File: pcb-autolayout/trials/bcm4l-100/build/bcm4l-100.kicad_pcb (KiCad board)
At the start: 4 copper layers, 80 x 60 mm, 128 parts, among them J1 MicroFit 2x4, J2 MicroFit 2x6, J3 SWD, Q1 SQD40P06 (P-MOS), Q11 ZXMP6A13F -60V, Q12 MMBT3904, Q13 ZXMP6A13F -60V, Q14 MMBT3904, Q15 ZXMP6A13F -60V, Q16 MMBT3904, Q17 ZXMP6A13F -60V, Q18 MMBT3904, SW1 RESET, U1 LMR16006X-Q1, U2 TLV1117LV33-Q1, U3 TJA1051T/3, U4 TJA1021T/20, U5 STM32F103C8T6, Y1 8MHz

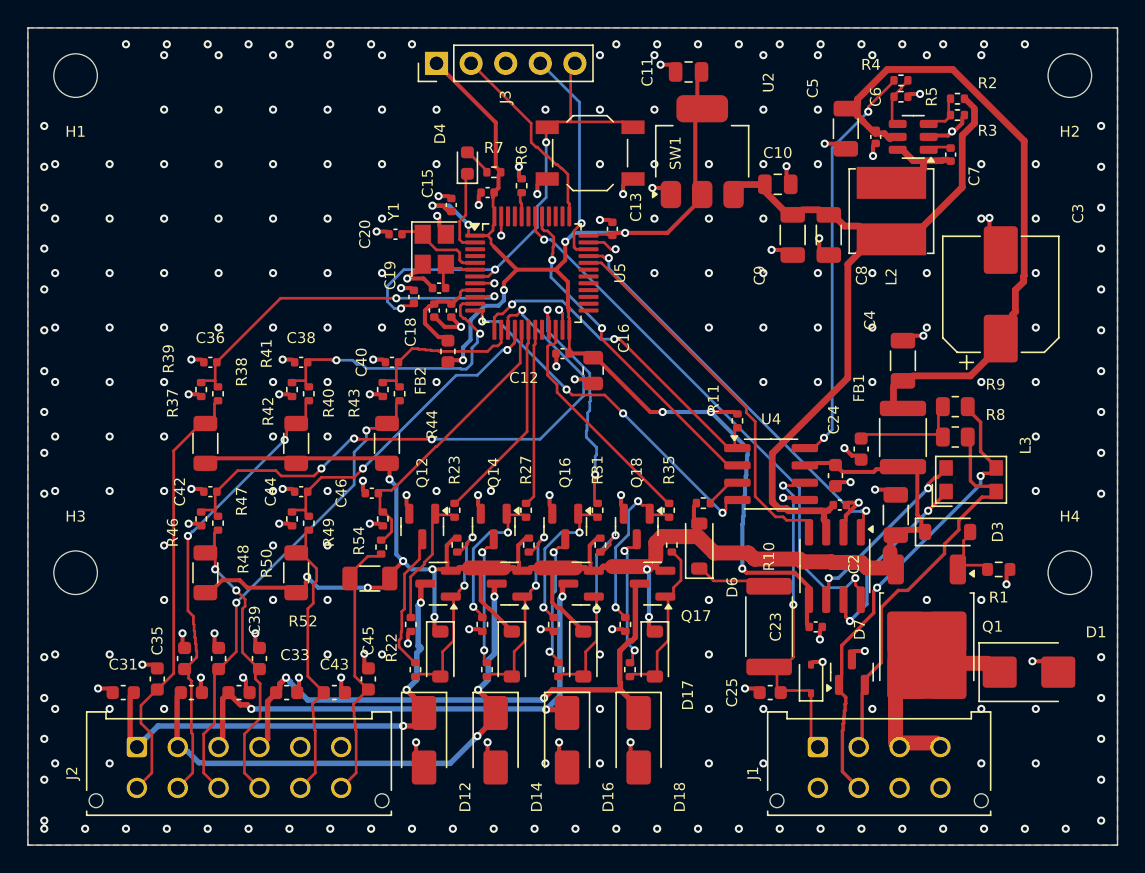
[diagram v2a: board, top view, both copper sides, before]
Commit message: pcb-autolayout: revert circuit to original, engine-computed netclasses
Circuit changes from round 3 reverted (circuit is an input, owner's
decision); review findings moved to CIRCUIT-ISSUES.md. circuit.py now
only adds layout constraints (net attributes, keep_away, rots, near).

Engine: T08/T09 netclass compiler (IPC-2221 width, voltage-based
clearance, per-kind minimums, KiCad netclasses in .kicad_pro, table
build/netclasses.md, tests); per-net current; plane-island measurement
before dead-copper removal; I/O protection placed before blocks;
satellite halo for anchors; TPS54202 template; cascading rip-up with
best-state restore and cycle detection.

Trial on original circuit: KiCad DRC 0 errors, 13/16 rules; 1 open pin
caused by regional capacity (needs T34 placement repair).

Co-Authored-By: Claude Opus 5.5 <noreply@anthropic.com>
Claude-Session: https://claude.ai/code/session_012jwodCpQFB8wopi3P3TnUz
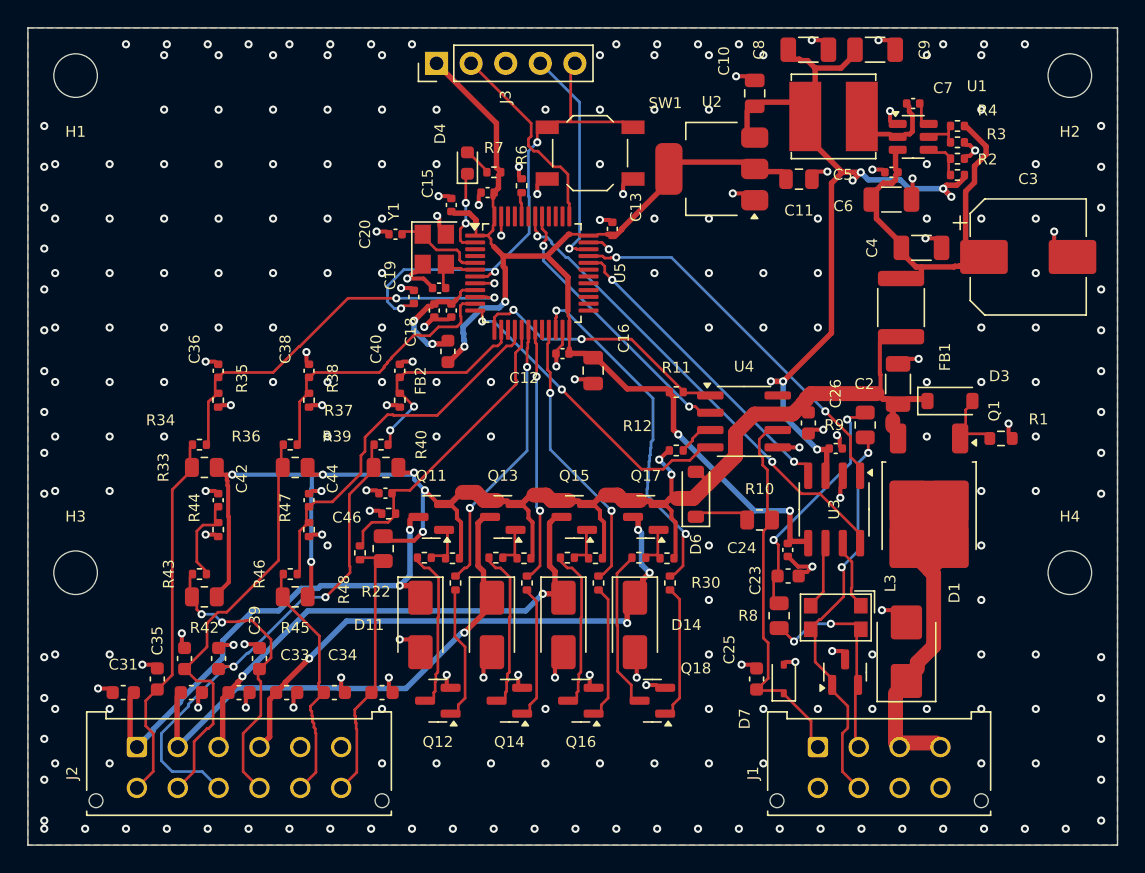
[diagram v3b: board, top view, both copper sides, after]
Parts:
- removed D17: BZT52C10, Diode_SMD:D_SOD-123
- removed the D3 at (167.5, 97.0)
- removed the D6 at (149.3, 98.0)
- removed the D7 at (157.5, 107.8)
- removed the R1 at (171.3, 99.8)
- removed the R10 at (154.4, 104.0)
- removed the R40 at (119.7, 90.5)
- removed the R49 at (119.7, 100.0)
- removed R52: 4k7, Resistor_SMD:R_1206_3216Metric
- removed the R8 at (168.1, 90.0)
- removed the R9 at (168.1, 87.8)
- added R34: 47k, Resistor_SMD:R_0402_1005Metric, F.Cu at (112.6, 90.6)
- added R35: 10k, Resistor_SMD:R_0402_1005Metric, F.Cu at (114.0, 87.3)
- added R44: 10k, Resistor_SMD:R_0402_1005Metric, F.Cu at (114.0, 96.8)
- C10: renamed from C11; value 22u -> 10u
- C11: renamed from C10; value 10u -> 22u
- C2, C6: value 100n 100V -> 100n 50V
- C20: renamed from C40; value 10n -> 20p
- C21: value 15p -> 20p
- C24: renamed from C26; value 100n 50V -> 4n7
- C26: renamed from C24; value 4n7 -> 100n 50V
- C3: value 47u 63V -> 47u 35V
- C4: value 2u2 100V -> 4u7 50V
- C40: renamed from C20; value 15p -> 10n
- C5: value 4u7 100V -> 10u 50V
- D1: value SMBJ33CA -> SMBJ24A
- D6: renamed from D11; value BZT52C10 -> BAS21
- D7: renamed from D15; value BZT52C10 -> ESD LIN; footprint Diode_SMD:D_SOD-123 -> Diode_SMD:D_SOD-323
- L2: value 22u -> 10u
- Q11, Q13, Q15, Q17: value ZXMP6A13F -60V -> AO3401A
- R1: renamed from R36; footprint Resistor_SMD:R_0402_1005Metric -> Resistor_SMD:R_0603_1608Metric
- R10: renamed from R5; value 100k -> 1k; footprint Resistor_SMD:R_0402_1005Metric -> Resistor_SMD:R_0805_2012Metric
- R11: renamed from R27; value 1k -> 4k7
- R2: renamed from R29; value 10k -> 100k
- R21: renamed from R50; value 82k -> 10k
- R22: renamed from R41; value 82k -> 10k
- R23: renamed from R53; value 82k -> 1k
- R26: renamed from R22; value 10k -> 1k
- R28: renamed from R23; value 1k -> 10k
- R29: renamed from R28; value 10k -> 1k
- R3: renamed from R31; value 1k -> 13k7
- R30: renamed from R7; value 1k -> 10k
- R32: renamed from R6; value 10k -> 1k
- R33: renamed from R35; value 1k -> 2k2; footprint Resistor_SMD:R_0402_1005Metric -> Resistor_SMD:R_0805_2012Metric
- R36: renamed from R12; value 10k -> 2k2; footprint Resistor_SMD:R_0402_1005Metric -> Resistor_SMD:R_0805_2012Metric
- R37, R43, R46: value 4k7 -> 47k; footprint Resistor_SMD:R_1206_3216Metric -> Resistor_SMD:R_0402_1005Metric
- R39: renamed from R4; value 10k -> 2k2; footprint Resistor_SMD:R_0402_1005Metric -> Resistor_SMD:R_0805_2012Metric
- R4: renamed from R32; value 10k -> 100k
- R40: renamed from R47; value 82k -> 47k
- R42: renamed from R34; value 10k -> 2k2; footprint Resistor_SMD:R_0402_1005Metric -> Resistor_SMD:R_0805_2012Metric
- R45: renamed from R33; value 10k -> 2k2; footprint Resistor_SMD:R_0402_1005Metric -> Resistor_SMD:R_0805_2012Metric
- R48: renamed from R11; value 4k7 -> 2k2; footprint Resistor_SMD:R_0402_1005Metric -> Resistor_SMD:R_0805_2012Metric
- R49: renamed from R38; value 82k -> 47k
- R5: renamed from R30; value 10k -> 22k
- R6: renamed from R44; value 82k -> 10k
- R7: renamed from R45; value 10k -> 1k
- R8: renamed from R2; value 100k -> 60R4; footprint Resistor_SMD:R_0402_1005Metric -> Resistor_SMD:R_0805_2012Metric
- R9: renamed from R3; value 18k -> 60R4; footprint Resistor_SMD:R_0402_1005Metric -> Resistor_SMD:R_0805_2012Metric
- U1: value LMR16006X-Q1 -> TPS54202
- U2: value TLV1117LV33-Q1 -> AMS1117-3.3
- moved R5 48.6 mm to (168.2, 68.4), turned to 0 degrees
- moved R39 47.3 mm to (126.3, 92.3), turned to 180 degrees
- moved R4 47.1 mm to (168.2, 67.2), turned to 180 degrees
- moved R8 40.1 mm to (155.2, 103.2), turned to 90 degrees
- moved R2 37.8 mm to (168.2, 70.8), turned to 180 degrees
- moved D3 37.1 mm to (167.7, 87.4), turned to 0 degrees
- moved R3 36.9 mm to (168.2, 69.6), turned to 0 degrees
- moved R33 34.3 mm to (113.0, 92.3), turned to 180 degrees
- moved R10 32.8 mm to (153.7, 96.1)
- moved R42 31.7 mm to (113.0, 101.8), turned to 180 degrees
- moved R32 31.1 mm to (147.1, 100.8), turned to -90 degrees
- moved R30 31.1 mm to (146.9, 98.9)
- moved R1 30.8 mm to (171.4, 90.1), turned to 0 degrees
- moved R36 30.1 mm to (119.6, 92.3)
- moved R45 27.9 mm to (119.6, 101.8), turned to 180 degrees
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- renumbered C9 to C8, C8 to C9, D12 to D11, D14 to D12, D16 to D13, D18 to D14, D13 to D3, R25 to R12, R54 to R25, R21 to R27, R26 to R31, R39 to R38, R51 to R41, R48 to R47, R42 to R50
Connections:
- C10 pad 1: +3V3 -> +5V
- C11 pad 1: +5V -> +3V3
- C20 pad 1: IN3_M -> OSC_IN
- C24 pad 1: VBAT_P -> CAN_SPL
- C26 pad 1: CAN_SPL -> VBAT_P
- C40 pad 1: OSC_IN -> IN3_M
- D3 pad 2: OUT2_G -> Q1_G
- D6 pad 1: VBAT_P -> LIN_PU
- D6 pad 2: OUT1_G -> VBAT_P
- D7 pad 1: VBAT_P -> LIN
- D7 pad 2: OUT3_G -> GND
- L3 pad 2: CANH -> CANL_T
- L3 pad 4: CANL_T -> CANH
- R1 pad 1: OUT4_B -> Q1_G
- R10 pad 1: EN5 -> LIN_PU
- R10 pad 2: GND -> LIN
- R11 pad 1: OUT2_M -> LIN_RX
- R11 pad 2: OUT2_B -> +3V3
- R12 pad 1: VBAT_P -> LIN_WAKE
- R12 pad 2: OUT2_G -> VBAT_P
- R2 pad 1: VBAT_P -> +5V
- R2 pad 2: OUT3_G -> FB5
- R21 pad 1: IN5 -> VBAT_P
- R21 pad 2: IN5_M -> OUT1_G
- R22 pad 1: IN2 -> OUT1_G
- R22 pad 2: IN2_M -> OUT1_C
- R23 pad 1: IN6 -> OUT1_M
- R23 pad 2: IN6_M -> OUT1_B
- R24 pad 1: OUT1_B -> VBAT_P
- R24 pad 2: GND -> OUT2_G
- R25 pad 1: IN6_M -> OUT2_G
- R25 pad 2: GND -> OUT2_C
- R26 pad 1: OUT1_G -> OUT2_M
- R26 pad 2: OUT1_C -> OUT2_B
- R27 pad 2: OUT1_G -> OUT3_G
- R28 pad 1: OUT1_M -> OUT3_G
- R28 pad 2: OUT1_B -> OUT3_C
- R29 pad 1: OUT2_B -> OUT3_M
- R29 pad 2: GND -> OUT3_B
- R3 pad 1: OUT3_M -> FB5
- R3 pad 2: OUT3_B -> GND
- R30 pad 1: +3V3 -> VBAT_P
- R30 pad 2: LED_A -> OUT4_G
- R31 pad 1: OUT2_G -> OUT4_G
- R31 pad 2: OUT2_C -> OUT4_C
- R32 pad 1: BOOT0 -> OUT4_M
- R32 pad 2: GND -> OUT4_B
- R33 pad 1: OUT4_M -> VBAT_P
- R33 pad 2: OUT4_B -> IN1
- R36 pad 1: LIN_WAKE -> VBAT_P
- R36 pad 2: VBAT_P -> IN2
- R37 pad 1: VBAT_P -> IN2
- R37 pad 2: IN1 -> IN2_M
- R38 pad 1: IN1_M -> IN2_M
- R39 pad 1: LIN_INH -> VBAT_P
- R39 pad 2: EN5 -> IN3
- R4 pad 1: OUT3_B -> VBAT_F
- R4 pad 2: GND -> EN5
- R40 pad 1: IN4 -> IN3
- R40 pad 2: IN4_M -> IN3_M
- R41 pad 1: IN5_M -> IN3_M
- R42 pad 1: OUT4_G -> VBAT_P
- R42 pad 2: OUT4_C -> IN4
- R43 pad 1: VBAT_P -> IN4
- R43 pad 2: IN3 -> IN4_M
- R45 pad 2: OUT4_G -> IN5
- R46 pad 1: VBAT_P -> IN5
- R46 pad 2: IN4 -> IN5_M
- R47 pad 1: IN4_M -> IN5_M
- R48 pad 1: LIN_RX -> VBAT_P
- R48 pad 2: +3V3 -> IN6
- R49 pad 1: IN1 -> IN6
- R49 pad 2: IN1_M -> IN6_M
- R5 pad 1: OUT3_G -> EN5
- R5 pad 2: OUT3_C -> GND
- R50 pad 1: IN2_M -> IN6_M
- R6 pad 1: IN3 -> BOOT0
- R6 pad 2: IN3_M -> GND
- R7 pad 1: IN3_M -> +3V3
- R7 pad 2: GND -> LED_A
- R8 pad 1: +5V -> CANH
- R8 pad 2: FB5 -> CAN_SPL
- R9 pad 1: FB5 -> CANL
- R9 pad 2: GND -> CAN_SPL
- U1 pad 1: BOOT5 -> GND
- U1 pad 2: GND -> SW5
- U1 pad 3: FB5 -> VBAT_F
- U1 pad 4: EN5 -> FB5
- U1 pad 5: VBAT_F -> EN5
- U1 pad 6: SW5 -> BOOT5
- U4 pad 8: LIN_INH -> (no net)
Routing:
- net IN4_M: track 41.9 -> 5.58 mm, vias 4 -> 0
- net LIN_INH: track 28.9 -> 0.00 mm, vias 2 -> 0
- net VBAT_F: track 40.8 -> 21.2 mm
- net +3V3: track 90.7 -> 74.7 mm, vias 9 -> 4
- net CANH: track 25.8 -> 12.8 mm, vias 0 -> 2
- net OUT3_G: track 14.5 -> 2.40 mm, vias 2 -> 0
- net OUT2_G: track 12.9 -> 2.40 mm, vias 2 -> 0
- net OUT1_G: track 12.9 -> 2.40 mm, vias 2 -> 0
- net CAN_SPL: track 6.50 -> 16.0 mm, vias 0 -> 2
- net OUT4_M: track 15.9 -> 25.3 mm, vias 0 -> 2
- net CANH_T: track 12.7 -> 3.69 mm, vias 2 -> 0
- net CANL_T: track 12.4 -> 3.55 mm, vias 2 -> 0
- net +5V: track 43.7 -> 51.8 mm, vias 0 -> 7
- net OUT4_G: track 10.2 -> 2.40 mm
- net VBAT_IN: track 9.30 -> 15.6 mm
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
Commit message: pcb-autolayout: seven phase skills + tools behind each
Skills: pcb-intake, pcb-part, pcb-constraints, pcb-place, pcb-route,
pcb-verify, pcb-release; pcb-autolayout becomes the orchestrator.

Tools:
- intake.py + pcbkit/sexpr.py: KiCad kicadsexpr netlist -> design.json
  (sheet = block, Layout_* fields); round-trip test, checked on a real
  KiCad 7 netlist (159/159 pins)
- verify.py: check an existing board (incl. hand-drawn) with the same
  rules; absolute pad geometry from the board (bottom side, any angle),
  real courtyard polygons; run on three KiCad demo boards
- release.py: gerber/drill/CPL/BOM/manifest behind a release gate that
  refuses unwaived severity-C failures
- constraints.py: netclass compile + attribute checks
- parts-db schema + parts_lint.py (one draft entry)
- run.py --until constraints|place|route
- netclass policy: inner-layer IPC-2221 width

Co-Authored-By: Claude Opus 5.5 <noreply@anthropic.com>
Claude-Session: https://claude.ai/code/session_012jwodCpQFB8wopi3P3TnUz
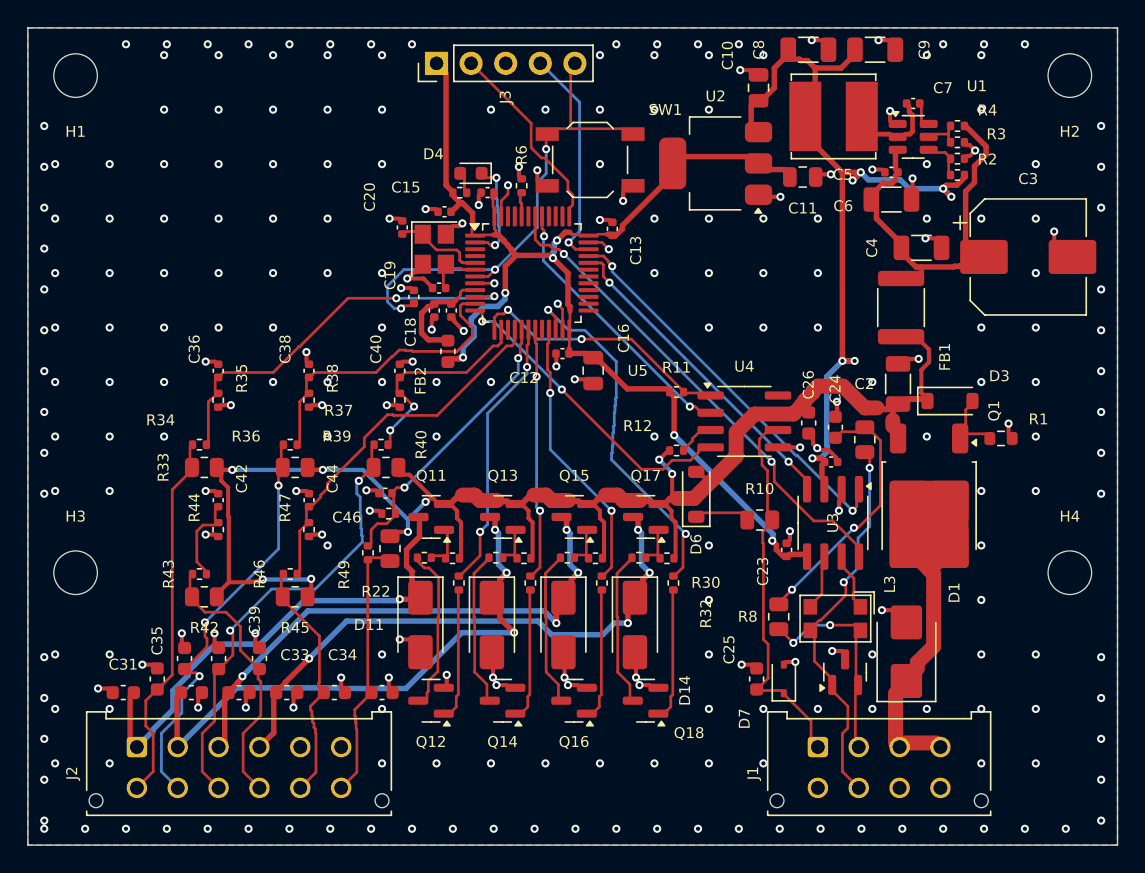
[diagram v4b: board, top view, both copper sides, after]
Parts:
- C20: renamed from C40; value 10n -> 20p
- C24: renamed from C26; value 100n 50V -> 4n7
- C26: renamed from C24; value 4n7 -> 100n 50V
- C40: renamed from C20; value 20p -> 10n
- Q11: renamed from Q12; value MMBT3904 -> AO3401A
- Q12: renamed from Q11; value AO3401A -> MMBT3904
- Q13: renamed from Q14; value MMBT3904 -> AO3401A
- Q14: renamed from Q13; value AO3401A -> MMBT3904
- Q15: renamed from Q16; value MMBT3904 -> AO3401A
- Q16: renamed from Q15; value AO3401A -> MMBT3904
- Q17: renamed from Q18; value MMBT3904 -> AO3401A
- Q18: renamed from Q17; value AO3401A -> MMBT3904
- moved Q11 13.5 mm to (129.6, 95.9)
- moved Q13 13.5 mm to (134.9, 95.9)
- moved Q15 13.5 mm to (140.1, 95.9)
- moved Q17 13.5 mm to (145.4, 95.9)
- moved Q12 13.5 mm to (129.6, 109.4)
- moved Q14 13.5 mm to (134.8, 109.4)
- moved Q16 13.5 mm to (140.1, 109.4)
- moved Q18 13.5 mm to (145.3, 109.4)
- moved C26 11.3 mm to (157.3, 89.0), turned to -90 degrees
- moved C20 10.5 mm to (127.5, 74.7)
- moved C40 10.0 mm to (127.3, 85.2), turned to 90 degrees
- moved R48 5.97 mm to (126.6, 98.2), turned to -90 degrees
- moved R39 5.96 mm to (126.3, 92.3), turned to 180 degrees
- moved R7 2.92 mm to (131.7, 72.1), turned to 0 degrees
- moved C24 2.01 mm to (159.3, 89.3), turned to 90 degrees
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- renumbered R48 to R39, R39 to R48
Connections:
- C20 pad 1: IN3_M -> OSC_IN
- C24 pad 1: VBAT_P -> CAN_SPL
- C26 pad 1: CAN_SPL -> VBAT_P
- C40 pad 1: OSC_IN -> IN3_M
- Q11 pad 1: OUT1_B -> OUT1_G
- Q11 pad 2: GND -> VBAT_P
- Q11 pad 3: OUT1_C -> OUT1
- Q12 pad 1: OUT1_G -> OUT1_B
- Q12 pad 2: VBAT_P -> GND
- Q12 pad 3: OUT1 -> OUT1_C
- Q13 pad 1: OUT2_B -> OUT2_G
- Q13 pad 2: GND -> VBAT_P
- Q13 pad 3: OUT2_C -> OUT2
- Q14 pad 1: OUT2_G -> OUT2_B
- Q14 pad 2: VBAT_P -> GND
- Q14 pad 3: OUT2 -> OUT2_C
- Q15 pad 1: OUT3_B -> OUT3_G
- Q15 pad 2: GND -> VBAT_P
- Q15 pad 3: OUT3_C -> OUT3
- Q16 pad 1: OUT3_G -> OUT3_B
- Q16 pad 2: VBAT_P -> GND
- Q16 pad 3: OUT3 -> OUT3_C
- Q17 pad 1: OUT4_B -> OUT4_G
- Q17 pad 2: GND -> VBAT_P
- Q17 pad 3: OUT4_C -> OUT4
- Q18 pad 1: OUT4_G -> OUT4_B
- Q18 pad 2: VBAT_P -> GND
- Q18 pad 3: OUT4 -> OUT4_C
- R39 pad 2: IN6 -> IN3
- R48 pad 2: IN3 -> IN6
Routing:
- net IN3: track 35.0 -> 31.0 mm
- net OUT2: track 34.9 -> 38.6 mm, vias 1 -> 3
- net IN4: track 19.1 -> 17.3 mm, vias 2 -> 0
- net IN2_M: track 18.8 -> 20.5 mm
- net LED_K: track 5.23 -> 6.84 mm
- net +3V3: track 74.7 -> 76.0 mm, vias 4 -> 6
- net CAN_TX: track 26.3 -> 27.6 mm
- net CAN_SPL: track 16.0 -> 17.2 mm
- net CAN_S: track 33.5 -> 34.7 mm
- net OUT3: track 35.2 -> 36.3 mm, vias 2 -> 4
- net CANL: track 26.2 -> 25.2 mm
- net IN6_M: track 20.4 -> 19.4 mm, vias 0 -> 2
- net CANL_T: track 3.55 -> 2.63 mm
- net CANH_T: track 3.69 -> 2.79 mm
- net VBAT_P: track 102.4 -> 101.6 mm
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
